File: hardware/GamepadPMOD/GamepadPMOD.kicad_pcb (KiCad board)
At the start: 2 copper layers, 22.3 x 73 mm, 80 parts, among them J3 10129382-912001BLF, J4 613012243121, J5 Conn_02x03_Odd_Even, SW1 434121025816, U1 CH32V003F4U6

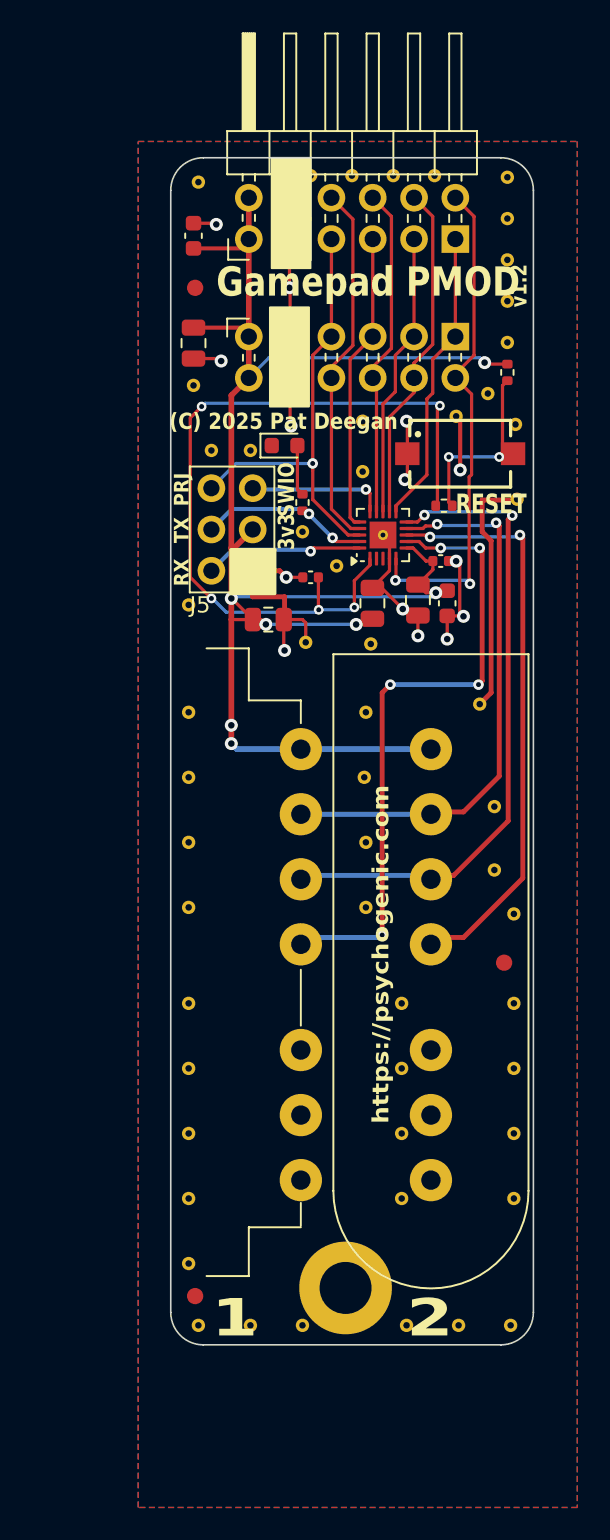
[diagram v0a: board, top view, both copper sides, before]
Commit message: PCB v1.3: TT designed for logo, slightly larger drill for SFC conn
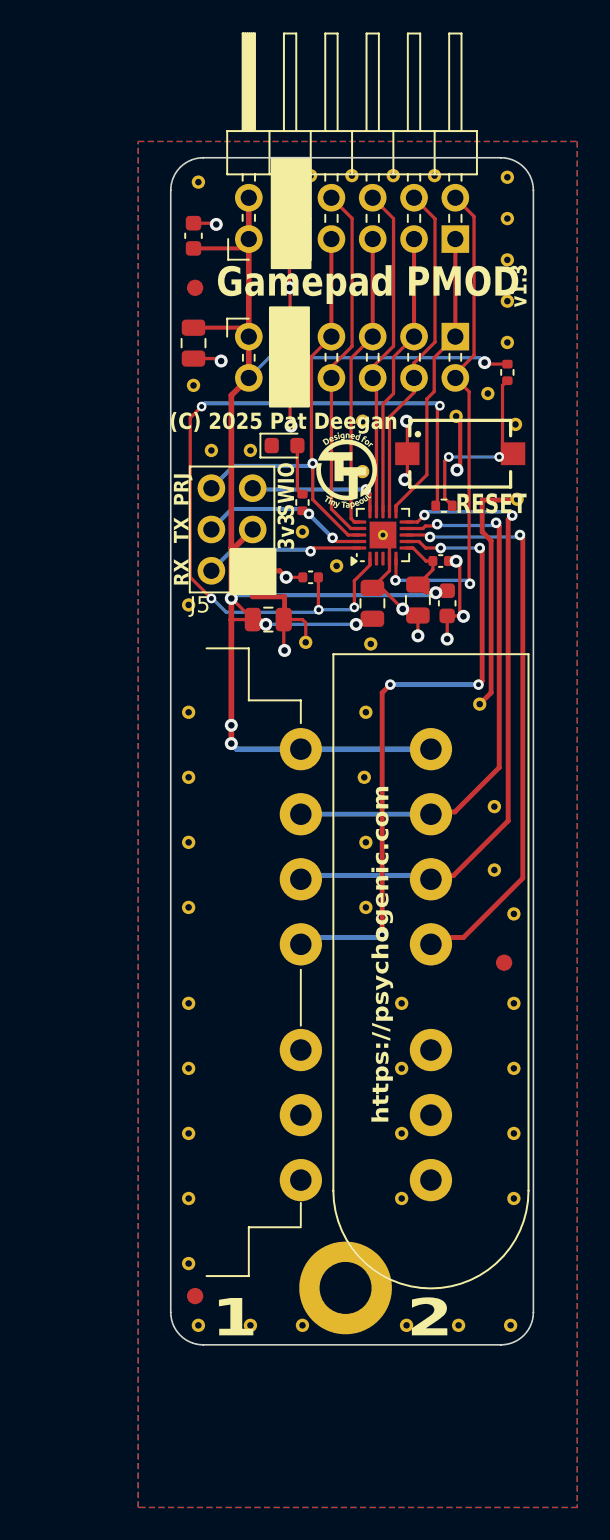
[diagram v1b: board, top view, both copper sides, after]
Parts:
- added LOGO1: PMOD_LOGO, TinyTapeout_PMOD:TT_PMOD_Logo_7mm, B.Cu at (27.1, 92.9)
- added REF**: TT_PMOD_Logo_5mm, TinyTapeout_PMOD:TT_PMOD_Logo_5mm, F.Cu at (31.6, 47.3)
- J1: value ~ -> SFC connector R/A
- J2: value ~ -> SFC connector VERT
- R3: value R_1k_0402 -> 200R
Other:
- board text added: "v1.3"
- board text removed: "v1.2"

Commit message: Modified pmod, breaking 1U width to allow for 2 vertical SFC connectors
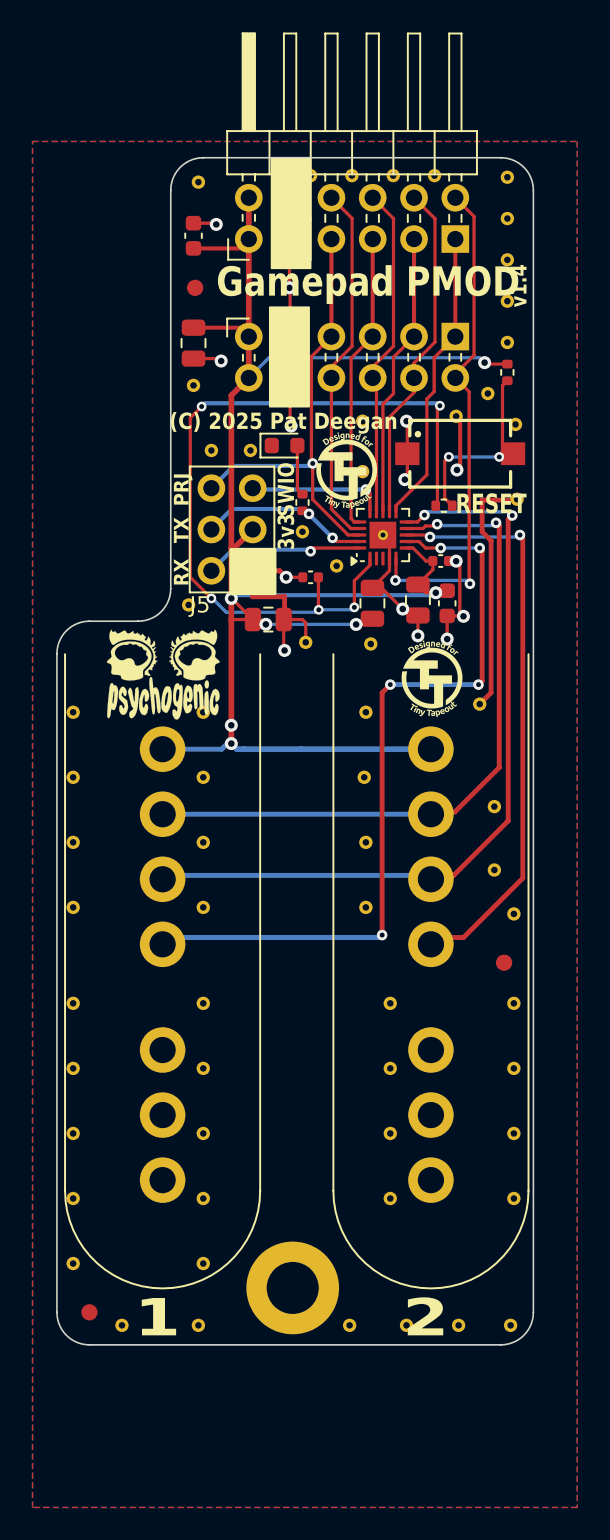
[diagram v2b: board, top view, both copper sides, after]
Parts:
- removed STITCH23: StitchingVia-0.4mmDrill, flyingcarsfootprints:StitchingVia-0.4mmDrill
- added G***: PsychoLogoMini, flyingcarsfootprints:PsychologoMini, F.Cu at (22.5, 56.8)
- added STITCH10: StitchingVia-0.4mmDrill, flyingcarsfootprints:StitchingVia-0.4mmDrill, F.Cu at (17.0, 85.0)
- added STITCH11: StitchingVia-0.4mmDrill, flyingcarsfootprints:StitchingVia-0.4mmDrill, F.Cu at (17.0, 81.0)
- added STITCH12: StitchingVia-0.4mmDrill, flyingcarsfootprints:StitchingVia-0.4mmDrill, F.Cu at (17.0, 77.0)
- added STITCH12: StitchingVia-0.4mmDrill, flyingcarsfootprints:StitchingVia-0.4mmDrill, F.Cu at (17.0, 71.1)
- added STITCH13: StitchingVia-0.4mmDrill, flyingcarsfootprints:StitchingVia-0.4mmDrill, F.Cu at (17.0, 67.1)
- added STITCH14: StitchingVia-0.4mmDrill, flyingcarsfootprints:StitchingVia-0.4mmDrill, F.Cu at (17.0, 63.1)
- added STITCH15: StitchingVia-0.4mmDrill, flyingcarsfootprints:StitchingVia-0.4mmDrill, F.Cu at (17.0, 59.1)
- added STITCH22: StitchingVia-0.4mmDrill, flyingcarsfootprints:StitchingVia-0.4mmDrill, F.Cu at (20.0, 96.8)
- added STITCH24: StitchingVia-0.4mmDrill, flyingcarsfootprints:StitchingVia-0.4mmDrill, F.Cu at (17.0, 89.0)
- added STITCH28: StitchingVia-0.4mmDrill, flyingcarsfootprints:StitchingVia-0.4mmDrill, F.Cu at (17.0, 93.0)
- added TTPMODLOGO: TT_PMOD_Logo_5mm, TinyTapeout_PMOD:TT_PMOD_Logo_5mm, F.Cu at (36.8, 60.1)
- J1: value SFC connector R/A -> SFC connector VERT
- moved LOGO1 13.1 mm to (30.2, 80.2)
- moved J1 8.50 mm to (22.5, 61.4)
- moved FID1 6.58 mm to (18.0, 96.0)
- moved STITCH22 6.10 mm to (34.0, 96.8)
- moved H1 3.25 mm to (30.5, 94.5)
- moved STITCH10 0.90 mm to (25.0, 85.0)
- moved STITCH11 0.90 mm to (25.0, 81.0)
- moved STITCH12 0.90 mm to (25.0, 71.1)
- moved STITCH12 0.90 mm to (25.0, 77.0)
- moved STITCH13 0.90 mm to (25.0, 67.1)
- moved STITCH14 0.90 mm to (25.0, 63.1)
- moved STITCH15 0.90 mm to (25.0, 59.1)
- moved STITCH24 0.90 mm to (25.0, 89.0)
- moved STITCH28 0.90 mm to (25.0, 93.0)
- moved STITCH12 0.70 mm to (36.5, 77.0)
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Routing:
- net /CTRL_LATCH: track 40.2 -> 48.7 mm
- net /CTRL_DAT1: track 39.5 -> 48.0 mm
- net /CTRL_CLK: track 34.3 -> 42.8 mm
- net +3V3: track 102.7 -> 107.0 mm
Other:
- board size 22.3 x 73 mm -> 29.3 x 73 mm
- board text added: "https://github.com/psychogenic/gamepad-pmod"
- board text added: "https://tinytapeout.com"
- board text added: "psychogenic.com"
- board text added: "v1.4"
- board text removed: "https://psychogenic.com"
- board text removed: "v1.3"
